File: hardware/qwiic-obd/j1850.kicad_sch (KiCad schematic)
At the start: 43 parts, among them J601 PIC ICSP, J602 PIC UART, Q601 DMG2301L, Q602 2N7002, Q603 2N7002, Q604 2N7002, Q605 2N7002, Q606 2N7002, Q607 2N7002, Q608 2N7002, Q609 2N7002, U601 LM317L_SOT-89, U602 NCS20072, U603 PIC16F15225-I{slash}ST

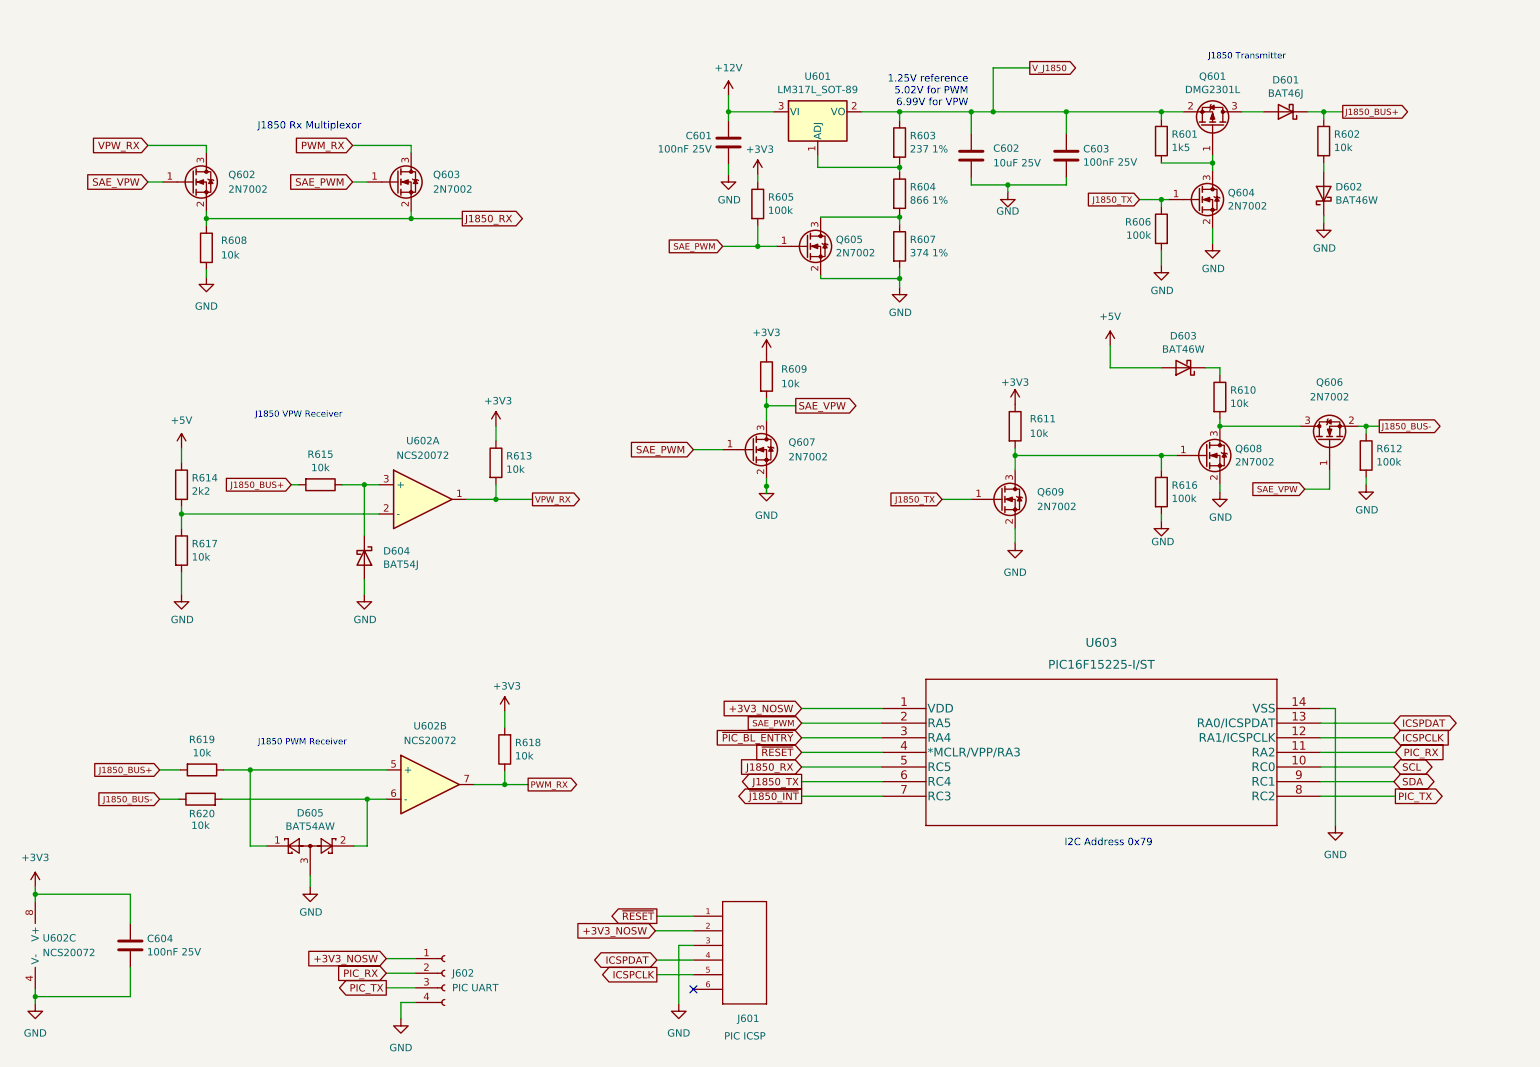
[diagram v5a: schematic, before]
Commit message: Added BL_LED on PA0, with a jumper
- if using ICSP, move jumper to 2,3 and PA0 is ISCPDAT
- if using bootloader, move jumper to 1,2 and PA0 is the LED
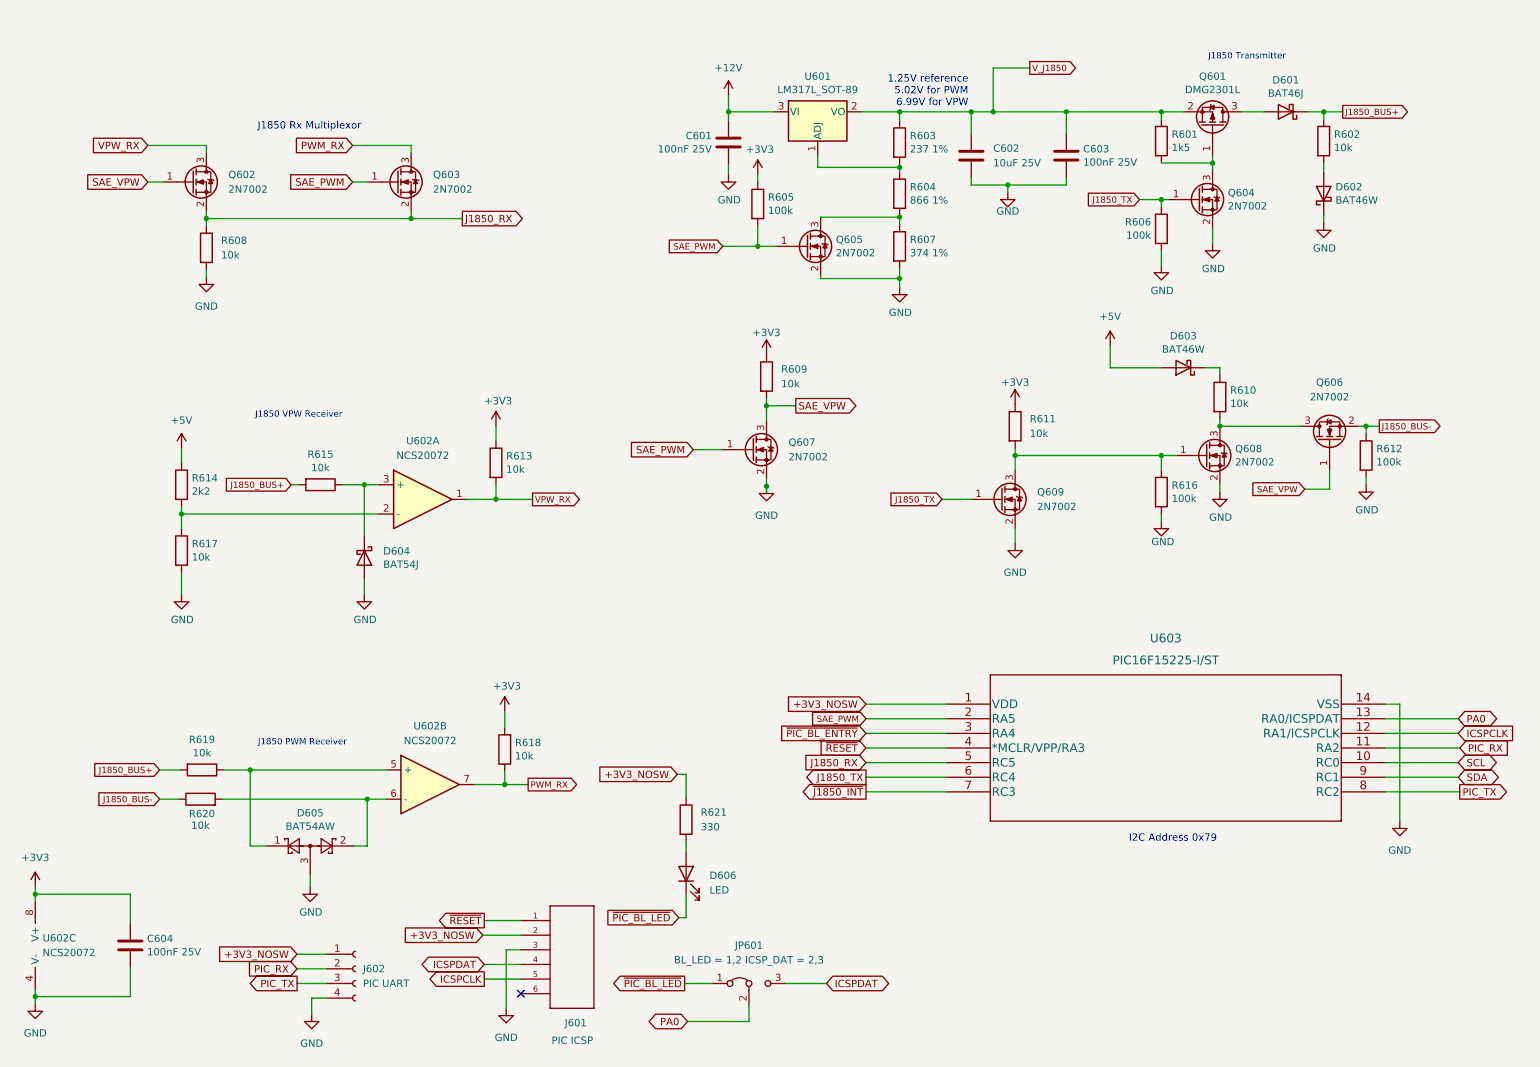
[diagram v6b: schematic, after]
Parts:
- added D606: LED, LED_SMD:LED_0805_2012Metric_Pad1.15x1.40mm_HandSolder, symbol Device:LED
- added JP601: BL_LED = 1,2 ICSP_DAT = 2,3, Connector_PinHeader_2.54mm:PinHeader_1x03_P2.54mm_Vertical, symbol Jumper:Jumper_3_Bridged12
- added R621: 330, Resistor_SMD:R_0805_2012Metric_Pad1.20x1.40mm_HandSolder, symbol Device:R
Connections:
- net +3V3_NOSW: now also R621.1
- net ICSPDAT: now also JP601.3 (B); no longer U603.13 (RA0/ICSPDAT)
- new net: D606.2 (A), R621.2
- new net PA0: JP601.2 (C), U603.13 (RA0/ICSPDAT)
- new net ~{PIC_BL_LED}: D606.1 (K), JP601.1 (A)
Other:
- moved on the sheet: J601, J602, U603

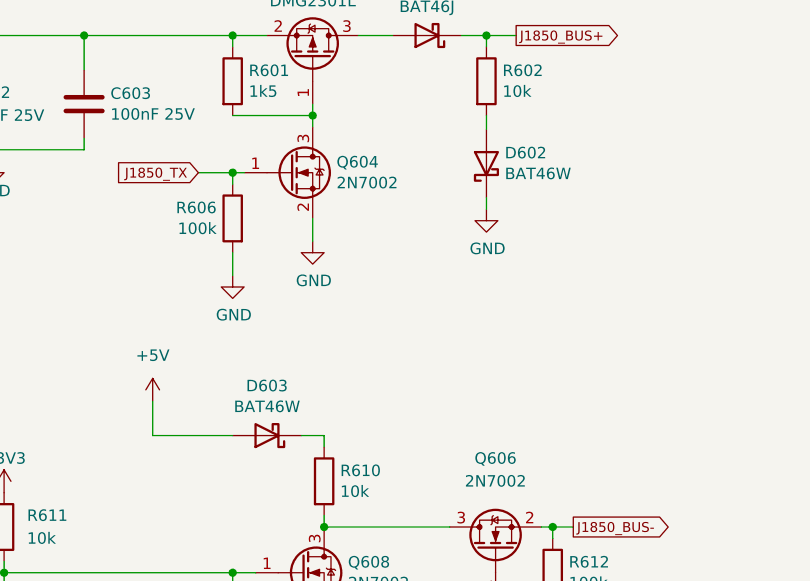
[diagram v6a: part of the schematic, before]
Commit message: Shrunk layout a bit
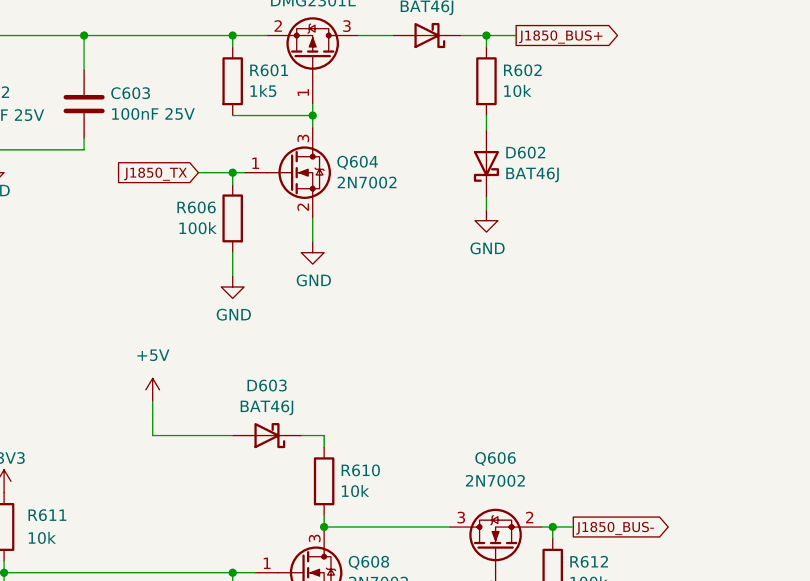
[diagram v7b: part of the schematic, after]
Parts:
- D602, D603: value BAT46W -> BAT46J
- J601: footprint SparkFun-Connectors:MOLEX-1X6 -> Connector_PinSocket_2.54mm:PinSocket_1x06_P2.54mm_Vertical
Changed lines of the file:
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@@
     (in_bom yes) (on_board yes)
     (property "Reference" "D603" (id 0) (at 223.52 71.9582 0))
-    (property "Value" "BAT46W" (id 1) (at 223.52 74.2696 0))
+    (property "Value" "BAT46J" (id 1) (at 223.52 74.2696 0))
     (property "Footprint" "Diode_SMD:D_SOD-123" (id 2) (at 223.52 73.025 0)
       (effects (font (size 1.27 1.27)) hide)
@@
       (effects (font (size 1.27 1.27)) (justify right))
     )
-    (property "Value" "BAT46W" (id 1) (at 249.936 48.387 90)
+    (property "Value" "BAT46J" (id 1) (at 249.936 48.387 90)
       (effects (font (size 1.27 1.27)) (justify right))
     )
@@
       (effects (font (size 1.27 1.27)) (justify right))
     )
-    (property "Footprint" "SparkFun-Connectors:MOLEX-1X6" (id 2) (at 115.316 184.912 0)
+    (property "Footprint" "Connector_PinSocket_2.54mm:PinSocket_1x06_P2.54mm_Vertical" (id 2) (at 115.316 184.912 0)
       (effects (font (size 0.508 0.508)) hide)
     )

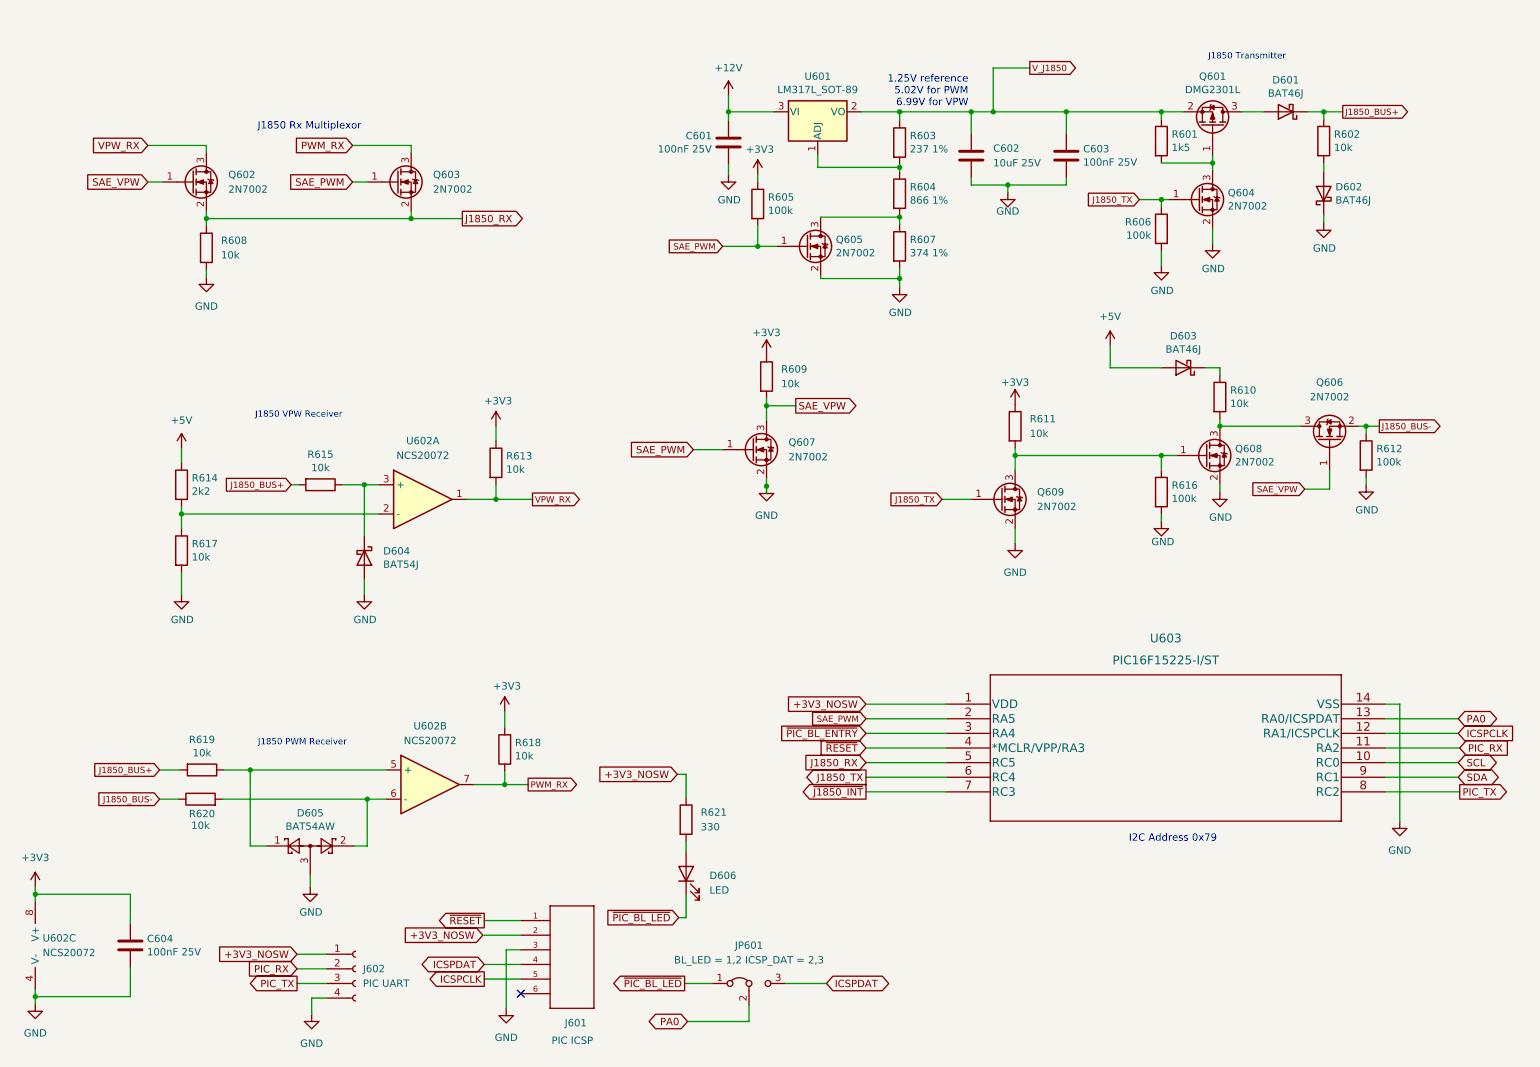
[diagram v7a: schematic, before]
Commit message: Switch out the PIC for an ATtiny424.
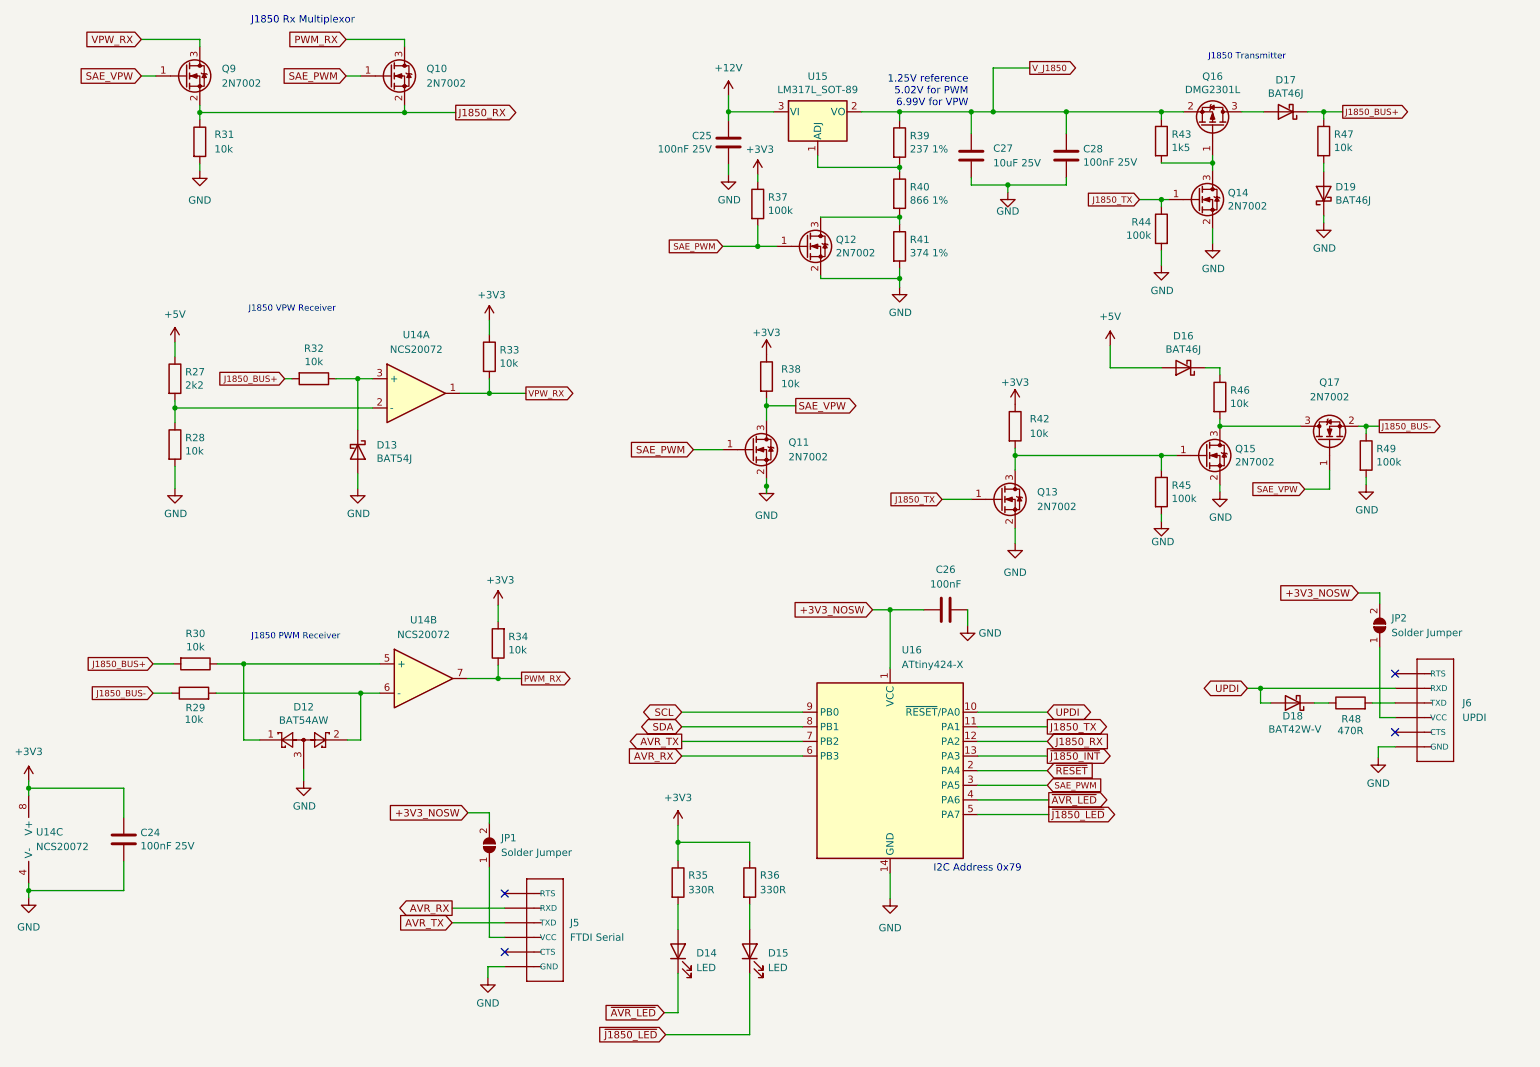
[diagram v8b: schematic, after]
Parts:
- removed D606: LED, LED_SMD:LED_0805_2012Metric_Pad1.15x1.40mm_HandSolder, symbol Device:LED
- removed J601: PIC ICSP, Connector_PinSocket_2.54mm:PinSocket_1x06_P2.54mm_Vertical, symbol SparkFun-Connectors:PIC-ICSPPOLAR_LOCK
- removed J602: PIC UART, Connector_PinHeader_2.54mm:PinHeader_1x04_P2.54mm_Vertical, symbol Connector:Conn_01x04_Female
- removed JP601: BL_LED = 1,2 ICSP_DAT = 2,3, Connector_PinHeader_2.54mm:PinHeader_1x03_P2.54mm_Vertical, symbol Jumper:Jumper_3_Bridged12
- removed R621: 330, Resistor_SMD:R_0805_2012Metric_Pad1.20x1.40mm_HandSolder, symbol Device:R
- removed U603: PIC16F15225-I/ST, UltraLibrarian:PIC16F15225-I&slash_ST, symbol UltraLibrarian:PIC16F15225-I{brace}slash}ST
- added C26: 100nF, Capacitor_SMD:C_0805_2012Metric_Pad1.18x1.45mm_HandSolder, symbol Device:C
- added D14, D15: LED, LED_SMD:LED_0805_2012Metric_Pad1.15x1.40mm_HandSolder, symbol Device:LED
- added D18: BAT42W-V, Diode_SMD:D_SOD-123, symbol Diode:BAT42W-V
- added J5: FTDI Serial, FTDI_BASIC, symbol Beirdo:FTDI_BASICPTH
- added J6: UPDI, FTDI_BASIC, symbol Beirdo:FTDI_BASICPTH
- added JP1, JP2: Solder Jumper, Jumper:SolderJumper-2_P1.3mm_Open_TrianglePad1.0x1.5mm, symbol Jumper:SolderJumper_2_Open
- added R35, R36: 330R, Resistor_SMD:R_0805_2012Metric_Pad1.20x1.40mm_HandSolder, symbol Device:R
- added R48: 470R, Resistor_SMD:R_0805_2012Metric_Pad1.20x1.40mm_HandSolder, symbol Device:R
- added U16: ATtiny424-X, Package_SO:TSSOP-14_4.4x5mm_P0.65mm, symbol MCU_Microchip_ATtiny:ATtiny424-X
- renumbered C604 to C24, C601 to C25, C602 to C27, C603 to C28, D605 to D12, D604 to D13, D603 to D16, D601 to D17, D602 to D19, Q603 to Q10, Q607 to Q11, Q605 to Q12, Q609 to Q13, Q604 to Q14, Q608 to Q15, Q601 to Q16, Q606 to Q17, Q602 to Q9, R614 to R27, R617 to R28, R620 to R29, R619 to R30, R608 to R31, R615 to R32, R613 to R33, R618 to R34, R605 to R37, R609 to R38, R603 to R39, R604 to R40, R607 to R41, R611 to R42, R601 to R43, R606 to R44, R616 to R45, R610 to R46, R602 to R47, R612 to R49, U602 to U14, U601 to U15
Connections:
- net +3V3: now also R35.1, R36.1
- net +3V3_NOSW: now also C26.2, JP1.2 (B), JP2.2 (B), U16.1 (VCC)
- net GND: now also C26.1, J5.1 (GND), J6.1 (GND), U16.14 (GND)
- net J1850_RX: now also U16.12 (PA2)
- net J1850_TX: now also U16.11 (PA1)
- net SAE_PWM: now also U16.3 (PA5)
- net SCL: now also U16.9 (PB0)
- net SDA: now also U16.8 (PB1)
- net ~{J1850_INT}: now also U16.13 (PA3)
- net ~{RESET}: now also U16.2 (PA4)
- new net: J5.3 (VCC), JP1.1 (A)
- new net: D18.1 (K), R48.1
- new net: J6.4 (TXD), R48.2
- new net: J6.3 (VCC), JP2.1 (A)
- new net: D15.2 (A), R36.2
- new net: D14.2 (A), R35.2
- new net AVR_RX: J5.5 (RXD), U16.6 (PB3)
- new net AVR_TX: J5.4 (TXD), U16.7 (PB2)
- new net UPDI: D18.2 (A), J6.5 (RXD), U16.10 (~{RESET}/PA0)
- new net ~{AVR_LED}: D14.1 (K), U16.4 (PA6)
- new net ~{J1850_LED}: D15.1 (K), U16.5 (PA7)
- no-connect marks 1 -> 4
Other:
- moved on the sheet: C24, D12, D13, Q10, Q9, R27, R28, R29, R30, R31, R32, R33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
